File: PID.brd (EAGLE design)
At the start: 70 x 44 mm, 37 parts, among them IC1 UA741CPE4, IC2 UA741CPE4, IC3 UA741CPE4, IC4 UA741CPE4, IC5 UA741CPE4

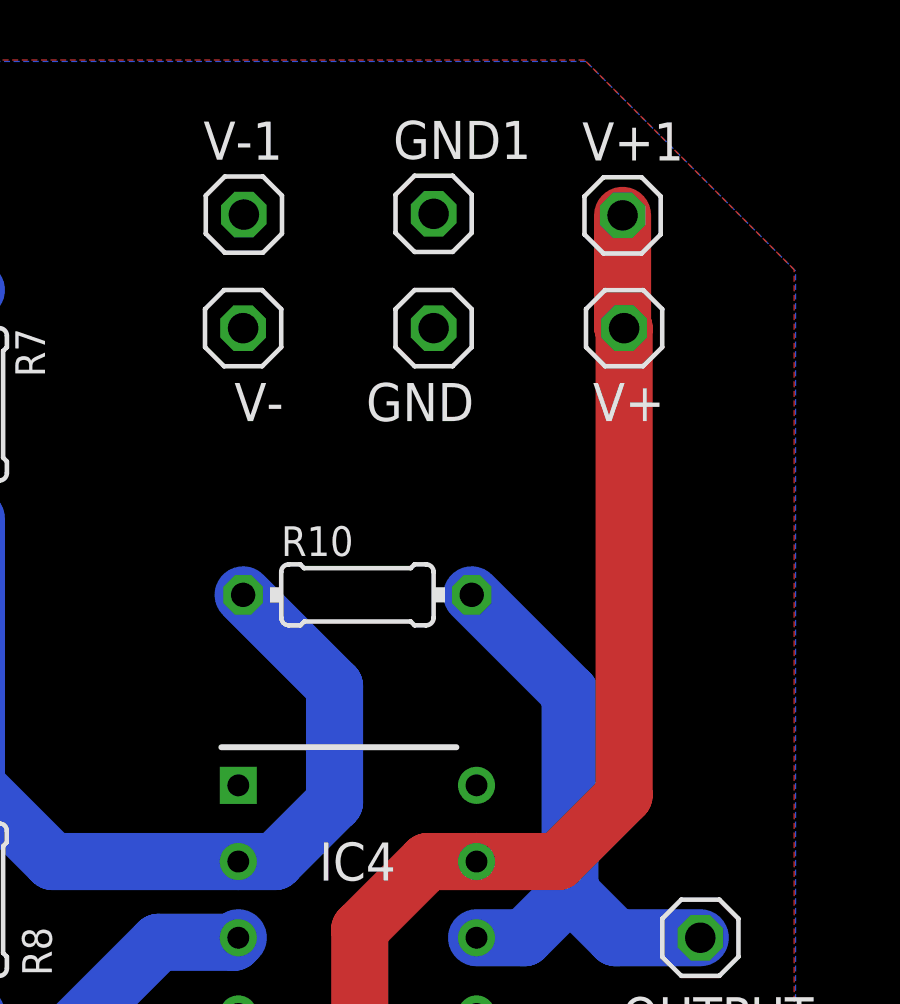
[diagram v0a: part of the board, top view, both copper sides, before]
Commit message: Le routage de lavage, tous les signaux sur le bottom, le plan de masse sur le bottom, plan de V- sur le top et routage du V+ sur le top
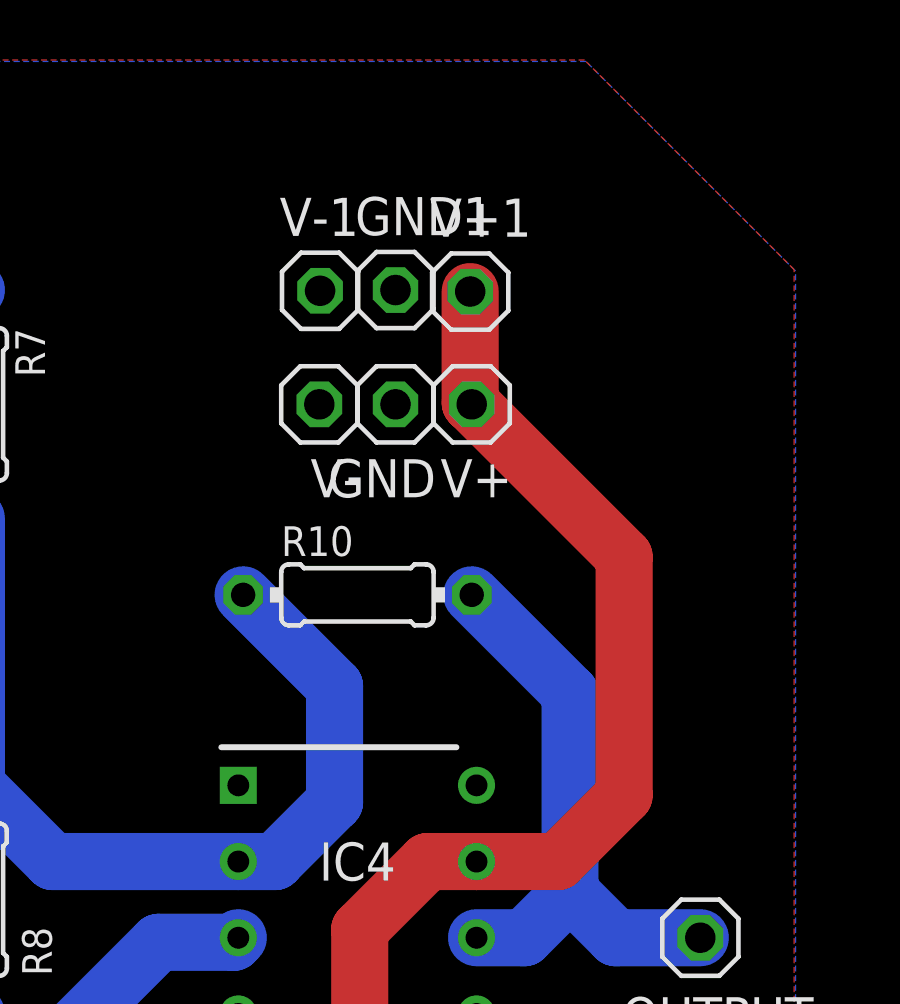
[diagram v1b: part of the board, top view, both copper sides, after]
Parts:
- moved V+ 5.68 mm to (87.6, 41.9)
- moved V+1 5.68 mm to (87.6, 45.7)
- moved V-1 3.59 mm to (82.6, 45.7)
- moved V- 3.59 mm to (82.5, 41.9)
- moved GND 2.84 mm to (85.1, 41.9)
- moved GND1 2.84 mm to (85.1, 45.7)
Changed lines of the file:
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@@
 <setting verticaltext="up"/>
 </settings>
-<grid distance="100" unitdist="mil" unit="mm" style="lines" multiple="1" display="yes" altdistance="5" altunitdist="mil" altunit="mil"/>
+<grid distance="100" unitdist="mil" unit="mil" style="lines" multiple="1" display="yes" altdistance="50" altunitdist="mil" altunit="mil"/>
 <layers>
 <layer number="1" name="Top" color="4" fill="1" visible="yes" active="yes"/>
@@
 <attribute name="VALUE" x="93.98" y="20.955" size="1.27" layer="27"/>
 </element>
-<element name="V-" library="pinhead" library_urn="urn:adsk.eagle:library:325" package="1X01" package3d_urn="urn:adsk.eagle:package:22485/2" value="" x="80.01" y="44.45" smashed="yes" rot="R180">
-<attribute name="NAME" x="81.3562" y="42.6212" size="1.27" layer="25" ratio="10" rot="R180"/>
-<attribute name="POPULARITY" value="64" x="80.01" y="44.45" size="1.778" layer="27" rot="R180" display="off"/>
-<attribute name="VALUE" x="81.28" y="47.625" size="1.27" layer="27" rot="R180"/>
-</element>
-<element name="V+" library="pinhead" library_urn="urn:adsk.eagle:library:325" package="1X01" package3d_urn="urn:adsk.eagle:package:22485/2" value="" x="92.71" y="44.45" smashed="yes" rot="R180">
-<attribute name="NAME" x="94.0562" y="42.6212" size="1.27" layer="25" ratio="10" rot="R180"/>
-<attribute name="POPULARITY" value="64" x="92.71" y="44.45" size="1.778" layer="27" rot="R180" display="off"/>
-<attribute name="VALUE" x="93.98" y="47.625" size="1.27" layer="27" rot="R180"/>
-</element>
-<element name="GND" library="pinhead" library_urn="urn:adsk.eagle:library:325" package="1X01" package3d_urn="urn:adsk.eagle:package:22485/2" value="" x="86.36" y="44.45" smashed="yes" rot="R180">
-<attribute name="NAME" x="87.7062" y="42.6212" size="1.27" layer="25" ratio="10" rot="R180"/>
-<attribute name="POPULARITY" value="64" x="86.36" y="44.45" size="1.778" layer="27" rot="R180" display="off"/>
-<attribute name="VALUE" x="87.63" y="47.625" size="1.27" layer="27" rot="R180"/>
+<element name="V-" library="pinhead" library_urn="urn:adsk.eagle:library:325" package="1X01" package3d_urn="urn:adsk.eagle:package:22485/2" value="" x="82.55" y="41.91" smashed="yes" rot="R180">
+<attribute name="NAME" x="83.8962" y="40.0812" size="1.27" layer="25" ratio="10" rot="R180"/>
+<attribute name="POPULARITY" value="64" x="82.55" y="41.91" size="1.778" layer="27" rot="R180" display="off"/>
+<attribute name="VALUE" x="83.82" y="45.085" size="1.27" layer="27" rot="R180"/>
+</element>
+<element name="V+" library="pinhead" library_urn="urn:adsk.eagle:library:325" package="1X01" package3d_urn="urn:adsk.eagle:package:22485/2" value="" x="87.63" y="41.91" smashed="yes" rot="R180">
+<attribute name="NAME" x="88.9762" y="40.0812" size="1.27" layer="25" ratio="10" rot="R180"/>
+<attribute name="POPULARITY" value="64" x="87.63" y="41.91" size="1.778" layer="27" rot="R180" display="off"/>
+<attribute name="VALUE" x="88.9" y="45.085" size="1.27" layer="27" rot="R180"/>
+</element>
+<element name="GND" library="pinhead" library_urn="urn:adsk.eagle:library:325" package="1X01" package3d_urn="urn:adsk.eagle:package:22485/2" value="" x="85.09" y="41.91" smashed="yes" rot="R180">
+<attribute name="NAME" x="86.4362" y="40.0812" size="1.27" layer="25" ratio="10" rot="R180"/>
+<attribute name="POPULARITY" value="64" x="85.09" y="41.91" size="1.778" layer="27" rot="R180" display="off"/>
+<attribute name="VALUE" x="86.36" y="45.085" size="1.27" layer="27" rot="R180"/>
 </element>
 <element name="JP1" library="pinhead" library_urn="urn:adsk.eagle:library:325" package="1X02" package3d_urn="urn:adsk.eagle:package:22435/2" value="" x="63.5" y="41.91" smashed="yes" rot="R270">
@@
 <attribute name="VALUE" x="15.7226" y="11.0744" size="0.9906" layer="27" ratio="10" rot="R90"/>
 </element>
-<element name="V-1" library="pinhead" library_urn="urn:adsk.eagle:library:325" package="1X01" package3d_urn="urn:adsk.eagle:package:22485/2" value="" x="80.0354" y="48.2346" smashed="yes">
-<attribute name="NAME" x="78.6892" y="50.0634" size="1.27" layer="25" ratio="10"/>
-<attribute name="POPULARITY" value="64" x="75.7936" y="53.2384" size="1.778" layer="27" display="off"/>
-<attribute name="VALUE" x="78.7654" y="45.0596" size="1.27" layer="27"/>
-</element>
-<element name="V+1" library="pinhead" library_urn="urn:adsk.eagle:library:325" package="1X01" package3d_urn="urn:adsk.eagle:package:22485/2" value="" x="92.6592" y="48.2092" smashed="yes">
-<attribute name="NAME" x="91.313" y="50.038" size="1.27" layer="25" ratio="10"/>
-<attribute name="POPULARITY" value="64" x="92.6592" y="48.2092" size="1.778" layer="27" display="off"/>
-<attribute name="VALUE" x="91.3892" y="45.0342" size="1.27" layer="27"/>
-</element>
-<element name="GND1" library="pinhead" library_urn="urn:adsk.eagle:library:325" package="1X01" package3d_urn="urn:adsk.eagle:package:22485/2" value="" x="86.36" y="48.26" smashed="yes">
-<attribute name="NAME" x="85.0138" y="50.0888" size="1.27" layer="25" ratio="10"/>
-<attribute name="POPULARITY" value="64" x="86.36" y="38.2524" size="1.778" layer="27" display="off"/>
-<attribute name="VALUE" x="85.09" y="45.085" size="1.27" layer="27"/>
+<element name="V-1" library="pinhead" library_urn="urn:adsk.eagle:library:325" package="1X01" package3d_urn="urn:adsk.eagle:package:22485/2" value="" x="82.5754" y="45.6946" smashed="yes">
+<attribute name="NAME" x="81.2292" y="47.5234" size="1.27" layer="25" ratio="10"/>
+<attribute name="POPULARITY" value="64" x="78.3336" y="50.6984" size="1.778" layer="27" display="off"/>
+<attribute name="VALUE" x="81.3054" y="42.5196" size="1.27" layer="27"/>
+</element>
+<element name="V+1" library="pinhead" library_urn="urn:adsk.eagle:library:325" package="1X01" package3d_urn="urn:adsk.eagle:package:22485/2" value="" x="87.5792" y="45.6692" smashed="yes">
+<attribute name="NAME" x="86.233" y="47.498" size="1.27" layer="25" ratio="10"/>
+<attribute name="POPULARITY" value="64" x="87.5792" y="45.6692" size="1.778" layer="27" display="off"/>
+<attribute name="VALUE" x="86.3092" y="42.4942" size="1.27" layer="27"/>
+</element>
+<element name="GND1" library="pinhead" library_urn="urn:adsk.eagle:library:325" package="1X01" package3d_urn="urn:adsk.eagle:package:22485/2" value="" x="85.09" y="45.72" smashed="yes">
+<attribute name="NAME" x="83.7438" y="47.5488" size="1.27" layer="25" ratio="10"/>
+<attribute name="POPULARITY" value="64" x="85.09" y="35.7124" size="1.778" layer="27" display="off"/>
+<attribute name="VALUE" x="83.82" y="42.545" size="1.27" layer="27"/>
 </element>
 </elements>
@@
 <contactref element="IC4" pad="7"/>
 <contactref element="V+" pad="1"/>
-<wire x1="92.71" y1="28.8798" x2="92.71" y2="44.45" width="1.905" layer="1"/>
 <wire x1="92.71" y1="28.8798" x2="90.5002" y2="26.67" width="1.905" layer="1"/>
 <wire x1="90.5002" y1="26.67" x2="87.79" y2="26.67" width="1.905" layer="1"/>
@@
 <wire x1="21.0312" y1="17.2974" x2="56.3118" y2="17.2974" width="1.905" layer="1"/>
 <contactref element="V+1" pad="1"/>
-<wire x1="92.6592" y1="48.2092" x2="92.6592" y2="44.5008" width="1.905" layer="1"/>
-<wire x1="92.6592" y1="44.5008" x2="92.71" y2="44.45" width="1.905" layer="1"/>
+<wire x1="87.5792" y1="45.6692" x2="87.5792" y2="41.9608" width="1.905" layer="1"/>
+<wire x1="87.5792" y1="41.9608" x2="87.63" y2="41.91" width="1.905" layer="1"/>
+<wire x1="92.71" y1="28.8798" x2="92.71" y2="36.83" width="1.905" layer="1"/>
+<wire x1="92.71" y1="36.83" x2="87.63" y2="41.91" width="1.905" layer="1"/>
 </signal>
 <signal name="N$2">
